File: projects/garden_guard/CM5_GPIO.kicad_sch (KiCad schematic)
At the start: 7 parts, among them J16 Conn_01x22_Female, J5 Conn_01x22_Female, J6 THD-02-R

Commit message: - Add 12V and 5V power sensing - Add solenoid and IR illum outputs, power expansion, an peripheral comms - General clean-up - Remove .bak files mistakenly added in previous commits - Add *.bak to .gitignore
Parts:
- removed J6: THD-02-R, Connector_PinHeader_2.54mm:PinHeader_2x02_P2.54mm_Vertical, symbol Connector_Generic:Conn_02x02_Odd_Even
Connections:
- net SCL1 is gone; now on net ID_SC: J16.20 (Pin_20), R7.2
- net SDA1 is gone; now on net ID_SD: J16.21 (Pin_21), R6.2
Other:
- note added: "CSI1 I2C Pull-Ups"
- note removed: "CSI1 Jumpers"
- note removed: "Jumper to enable CSI1 TODO: required?"
- note removed: "Jumpers to be fitted if DPHY1 is used"
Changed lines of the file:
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@@
 		(comment 4 "Adam Bowen")
 	)
-	(text "Jumper to enable CSI1\nTODO: required?"
+	(text "CSI1 I2C Pull-Ups"
 		(exclude_from_sim no)
-		(at 203.962 98.552 0)
-		(effects
-			(font
-				(size 1.27 1.27)
-				(thickness 0.1588)
-			)
-		)
-	)
-	(text "CSI1\nJumpers"
-		(exclude_from_sim no)
-		(at 179.324 102.362 0)
+		(at 193.04 103.632 0)
 		(effects
 			(font
@@
 		)
 	)
-	(text "Jumpers to be fitted if DPHY1 is used\n"
-		(exclude_from_sim no)
-		(at 223.52 130.556 0)
-		(effects
-			(font
-				(size 1.27 1.27)
-			)
-			(justify right bottom)
-		)
-	)
 	(text "CSI0"
 		(exclude_from_sim no)
@@
 		)
 	)
+	(text_box "CSI1 uses the HAT EEPROM ID I2C bus; we do not use HATs with this board, so we can use it.\n\nHAT ID bus does not have internal pull-up's specified, apply here."
+		(exclude_from_sim no)
+		(at 196.85 129.54 0)
+		(size 35.56 10.16)
+		(margins 0.9525 0.9525 0.9525 0.9525)
+		(stroke
+			(width 0)
+			(type solid)
+			(color 255 0 0 1)
+		)
+		(fill
+			(type none)
+		)
+		(effects
+			(font
+				(size 0.889 0.889)
+			)
+			(justify left)
+		)
+	)
 	(junction
 		(at 102.87 149.86)
@@
 	(polyline
 		(pts
-			(xy 177.8 93.98) (xy 228.6 93.98)
+			(xy 191.77 99.06) (xy 233.68 99.06)
 		)
 		(stroke
@@
 	(wire
 		(pts
-			(xy 198.12 106.68) (xy 208.28 106.68)
+			(xy 204.47 106.68) (xy 208.28 106.68)
 		)
 		(stroke
@@
 	(polyline
 		(pts
-			(xy 177.8 93.98) (xy 177.8 134.62)
+			(xy 191.77 99.06) (xy 191.77 140.97)
 		)
 		(stroke
@@
 	(polyline
 		(pts
-			(xy 177.8 134.62) (xy 228.6 134.62)
+			(xy 191.77 140.97) (xy 233.68 140.97)
 		)
 		(stroke
@@
 	(polyline
 		(pts
-			(xy 228.6 134.62) (xy 228.6 93.98)
+			(xy 233.68 140.97) (xy 233.68 93.98)
 		)
 		(stroke
@@
 	(wire
 		(pts
-			(xy 186.69 124.46) (xy 193.04 124.46)
-		)
-		(stroke
-			(width 0)
-			(type solid)
-		)
-	)
-	(wire
-		(pts
 			(xy 100.33 127) (xy 102.87 127)
 		)
@@
 	(wire
 		(pts
-			(xy 186.69 121.92) (xy 193.04 121.92)
-		)
-		(stroke
-			(width 0)
-			(type solid)
-		)
-	)
-	(wire
-		(pts
 			(xy 149.86 50.8) (xy 149.86 58.42)
 		)
@@
 		)
 	)
-	(label "ID_SC"
-		(at 192.405 121.92 180)
-		(effects
-			(font
-				(size 1.27 1.27)
-			)
-			(justify right bottom)
-		)
-	)
 	(label "DPHY1_D0_P"
 		(at 135.89 104.14 0)
@@
 		)
 	)
-	(label "SCL1"
-		(at 224.79 121.92 180)
-		(effects
-			(font
-				(size 1.27 1.27)
-			)
-			(justify right bottom)
-		)
-	)
 	(label "DPHY1_D2_P"
 		(at 116.84 147.32 180)
@@
 		)
 	)
-	(label "SDA1"
-		(at 135.89 149.86 0)
-		(effects
-			(font
-				(size 1.27 1.27)
-			)
-			(justify left bottom)
-		)
-	)
 	(label "DPHY0_D1_N"
 		(at 135.89 38.1 0)
@@
 		)
 	)
-	(label "SDA1"
-		(at 224.79 124.46 180)
-		(effects
-			(font
-				(size 1.27 1.27)
-			)
-			(justify right bottom)
-		)
-	)
 	(label "DPHY1_D2_N"
 		(at 116.84 144.78 180)
@@
 		)
 	)
-	(label "SCL1"
-		(at 135.89 147.32 0)
+	(label "ID_SD"
+		(at 135.89 149.86 0)
 		(effects
 			(font
@@
 		)
 	)
+	(label "ID_SC"
+		(at 135.89 147.32 0)
+		(effects
+			(font
+				(size 1.27 1.27)
+			)
+			(justify left bottom)
+		)
+	)
+	(label "ID_SC"
+		(at 205.74 121.92 180)
+		(effects
+			(font
+				(size 1.27 1.27)
+			)
+			(justify right bottom)
+		)
+	)
 	(label "DPHY1_C_N"
 		(at 135.89 116.84 0)
@@
 	)
 	(label "ID_SD"
-		(at 192.405 124.46 180)
+		(at 205.74 124.46 180)
 		(effects
 			(font
@@
 		)
 	)
+	(hierarchical_label "ID_SD"
+		(shape input)
+		(at 224.79 124.46 0)
+		(effects
+			(font
+				(size 1.27 1.27)
+			)
+			(justify left)
+		)
+	)
 	(hierarchical_label "SDA0"
 		(shape input)
@@
 		)
 	)
-	(hierarchical_label "ID_SD"
-		(shape input)
-		(at 186.69 124.46 180)
+	(hierarchical_label "PCIE_CLK_N"
+		(shape output)
+		(at 33.02 40.64 180)
 		(effects
 			(font
@@
 		)
 	)
-	(hierarchical_label "ID_SC"
+	(hierarchical_label "PCIE_RX_P"
 		(shape input)
-		(at 186.69 121.92 180)
-		(effects
-			(font
-				(size 1.27 1.27)
-			)
-			(justify right)
-		)
-	)
-	(hierarchical_label "PCIE_CLK_N"
-		(shape output)
-		(at 33.02 40.64 180)
+		(at 33.02 45.72 180)
 		(effects
 			(font
@@
 		)
 	)
-	(hierarchical_label "PCIE_RX_P"
+	(hierarchical_label "ID_SC"
 		(shape input)
-		(at 33.02 45.72 180)
+		(at 224.79 121.92 0)
 		(effects
 			(font
 				(size 1.27 1.27)
 			)
-			(justify right)
+			(justify left)
 		)
 	)
@@
 	(hierarchical_label "GPIO_VREF"
 		(shape input)
-		(at 198.12 106.68 180)
+		(at 204.47 106.68 180)
 		(effects
 			(font
@@
 				)
 			)
-		)
-	)
-	(symbol
-		(lib_id "Connector_Generic:Conn_02x02_Odd_Even")
-		(at 198.12 121.92 0)
-		(unit 1)
-		(exclude_from_sim no)
-		(in_bom yes)
-		(on_board yes)
-		(dnp no)
-		(property "Reference" "J6"
-			(at 195.453 116.713 0)
-			(effects
-				(font
-					(size 1.27 1.27)
-				)
-			)
-		)
-		(property "Value" "THD-02-R"
-			(at 199.39 118.7196 0)
-			(effects
-				(font
-					(size 1.27 1.27)
-				)
-			)
-		)
-		(property "Footprint" "Connector_PinHeader_2.54mm:PinHeader_2x02_P2.54mm_Vertical"
-			(at 198.12 121.92 0)
-			(effects
-				(font
-					(size 1.27 1.27)
-				)
-				(hide yes)
-			)
-		)
-		(property "Datasheet" "https://www.toby.co.uk/uploads/publications/1673.pdf"
-			(at 198.12 121.92 0)
-			(effects
-				(font
-					(size 1.27 1.27)
-				)
-				(hide yes)
-			)
-		)
-		(property "Description" ""
-			(at 198.12 121.92 0)
-			(effects
-				(font
-					(size 1.27 1.27)
-				)
-				(hide yes)
-			)
-		)
-		(property "Field4" "Toby"
-			(at 198.12 121.92 0)
-			(effects
-				(font
-					(size 1.27 1.27)
-				)
-				(hide yes)
-			)
-		)
-		(property "Field5" "THD-02-R"
-			(at 198.12 121.92 0)
-			(effects
-				(font
-					(size 1.27 1.27)
-				)
-				(hide yes)
-			)
-		)
-		(property "Field6" "151-604-425-761"
-			(at 198.12 121.92 0)
-			(effects
-				(font
-					(size 1.27 1.27)
-				)
-				(hide yes)
-			)
-		)
-		(property "Field7" "EDAC"
-			(at 198.12 121.92 0)
-			(effects
-				(font
-					(size 1.27 1.27)
-				)
-				(hide yes)
-			)
-		)
-		(property "Field8" "UCON00791"
-			(at 198.12 121.92 0)
-			(effects
-				(font
-					(size 1.27 1.27)
-				)
-				(hide yes)
-			)
-		)
-		(property "Part Description" "PinHeader_2x02_P2.54mm_Vertical"
-			(at 198.12 121.92 0)
-			(effects
-				(font
-					(size 1.27 1.27)
-				)
-				(hide yes)
-			)
-		)
-		(pin "1"
-		)
-		(pin "2"
-		)
-		(pin "3"
-		)
-		(pin "4"
-		)
-		(instances
-			(project "garden_guard"
-				(path "/dcdac9d4-ef08-426f-b97c-7b9219501e71/ffd8c860-2f3d-4401-ad04-ed468bcbcf5a"
-					(reference "J6")
-					(unit 1)
-				)
-			)

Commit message: - Add all missing footprints - Add specific part numbers to each component in schematic
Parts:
- renumbered J16 to J6, R6 to R10, R7 to R11, R8 to R9
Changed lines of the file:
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@@
 		(on_board yes)
 		(dnp no)
-		(property "Reference" "#PWR0130"
+		(property "Reference" "#PWR015"
 			(at 102.87 161.29 0)
 			(effects
@@
 			(project "garden_guard"
 				(path "/dcdac9d4-ef08-426f-b97c-7b9219501e71/ffd8c860-2f3d-4401-ad04-ed468bcbcf5a"
-					(reference "#PWR0130")
+					(reference "#PWR015")
 					(unit 1)
 				)
@@
 		(on_board yes)
 		(dnp no)
-		(property "Reference" "#PWR0131"
+		(property "Reference" "#PWR014"
 			(at 36.83 161.29 0)
 			(effects
@@
 			(project "garden_guard"
 				(path "/dcdac9d4-ef08-426f-b97c-7b9219501e71/ffd8c860-2f3d-4401-ad04-ed468bcbcf5a"
-					(reference "#PWR0131")
+					(reference "#PWR014")
 					(unit 1)
 				)
@@
 		(on_board yes)
 		(dnp no)
-		(property "Reference" "#PWR0134"
+		(property "Reference" "#PWR016"
 			(at 149.86 88.9 0)
 			(effects
@@
 			(project "garden_guard"
 				(path "/dcdac9d4-ef08-426f-b97c-7b9219501e71/ffd8c860-2f3d-4401-ad04-ed468bcbcf5a"
-					(reference "#PWR0134")
+					(reference "#PWR016")
 					(unit 1)
 				)
@@
 		(on_board yes)
 		(dnp no)
-		(property "Reference" "#PWR0135"
+		(property "Reference" "#PWR017"
 			(at 149.86 160.02 0)
 			(effects
@@
 			(project "garden_guard"
 				(path "/dcdac9d4-ef08-426f-b97c-7b9219501e71/ffd8c860-2f3d-4401-ad04-ed468bcbcf5a"
-					(reference "#PWR0135")
+					(reference "#PWR017")
 					(unit 1)
 				)
@@
 		(on_board yes)
 		(dnp no)
-		(property "Reference" "R6"
+		(property "Reference" "R10"
 			(at 203.708 111.125 0)
 			(effects
@@
 			(project "garden_guard"
 				(path "/dcdac9d4-ef08-426f-b97c-7b9219501e71/ffd8c860-2f3d-4401-ad04-ed468bcbcf5a"
-					(reference "R6")
+					(reference "R10")
 					(unit 1)
 				)
@@
 		(on_board yes)
 		(dnp no)
-		(property "Reference" "R7"
+		(property "Reference" "R11"
 			(at 217.678 111.125 0)
 			(effects
@@
 			(project "garden_guard"
 				(path "/dcdac9d4-ef08-426f-b97c-7b9219501e71/ffd8c860-2f3d-4401-ad04-ed468bcbcf5a"
-					(reference "R7")
+					(reference "R11")
 					(unit 1)
 				)
@@
 		(on_board yes)
 		(dnp no)
-		(property "Reference" "J16"
+		(property "Reference" "J6"
 			(at 134.62 95.25 0)
 			(effects
@@
 			(project "garden_guard"
 				(path "/dcdac9d4-ef08-426f-b97c-7b9219501e71/ffd8c860-2f3d-4401-ad04-ed468bcbcf5a"
-					(reference "J16")
+					(reference "J6")
 					(unit 1)
 				)
@@
 		(on_board yes)
 		(dnp no)
-		(property "Reference" "R8"
+		(property "Reference" "R9"
 			(at 137.795 137.16 90)
 			(effects
@@
 			(project "garden_guard"
 				(path "/dcdac9d4-ef08-426f-b97c-7b9219501e71/ffd8c860-2f3d-4401-ad04-ed468bcbcf5a"
-					(reference "R8")
+					(reference "R9")
 					(unit 1)
 				)

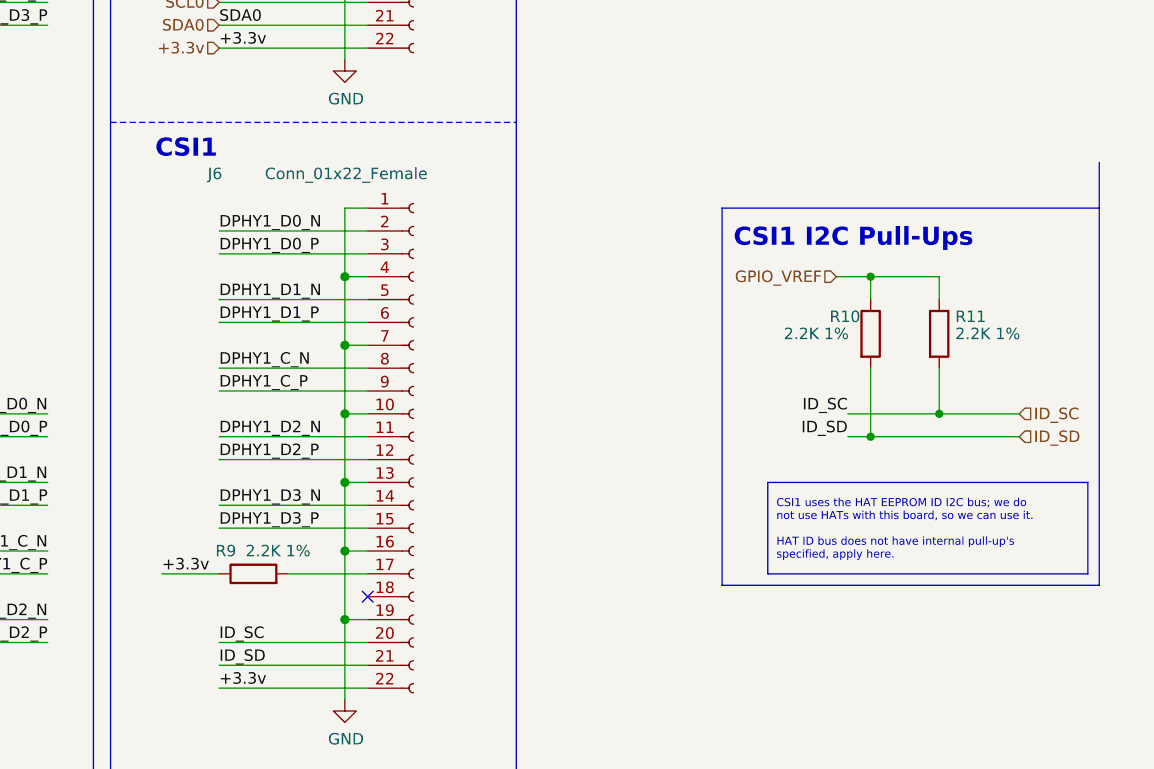
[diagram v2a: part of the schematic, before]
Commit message: - Find part numbers for CM5 parts - Minor CM5 symbol, footprint adjustments - Move to uniform small resistor and capacitor symbols - Add *lck to .gitignore
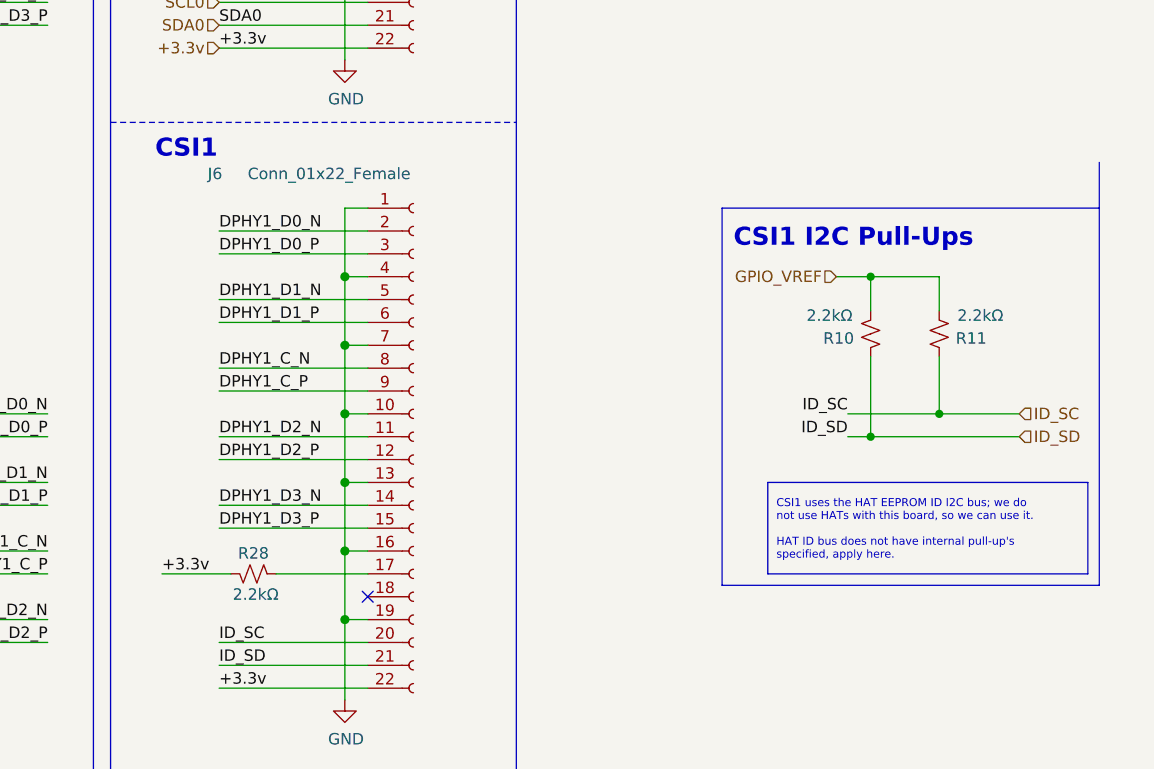
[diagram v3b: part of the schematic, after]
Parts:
- removed R10, R11, R9: 2.2K 1%, Resistor_SMD:R_0402_1005Metric, symbol Device:R
- added R10, R11, R28: 2.2kΩ, Capacitor_SMD:C_0603_1608Metric, symbol Device:R_Small_US
- J5, J6: MPN (none) -> FH12-22S-0.5SH(55); Mfr (none) -> Hirose
- Module1: MPN (none) -> 10164227-1004A1RLF; Mfr (none) -> Amphenol
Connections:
- net +3.3v: now also R28.2
- net GPIO_VREF: now also R10.1, R11.1
- net ID_SC: now also R11.2
- net ID_SD: now also R10.2
- net at J6.17 (Pin_17): now also R28.1

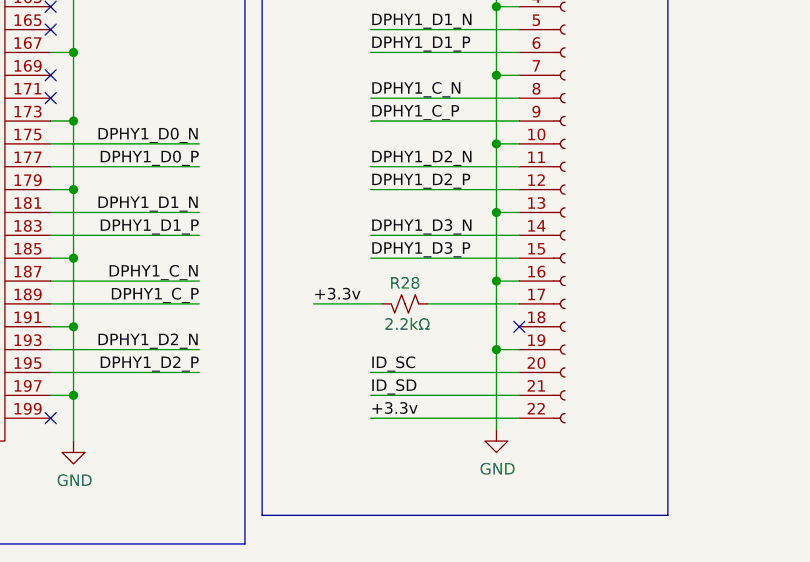
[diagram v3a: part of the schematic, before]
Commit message: - Assign 3D models to lingering footprints lacking them - Start playing with board layout - Move CM5 library files from project to components dir
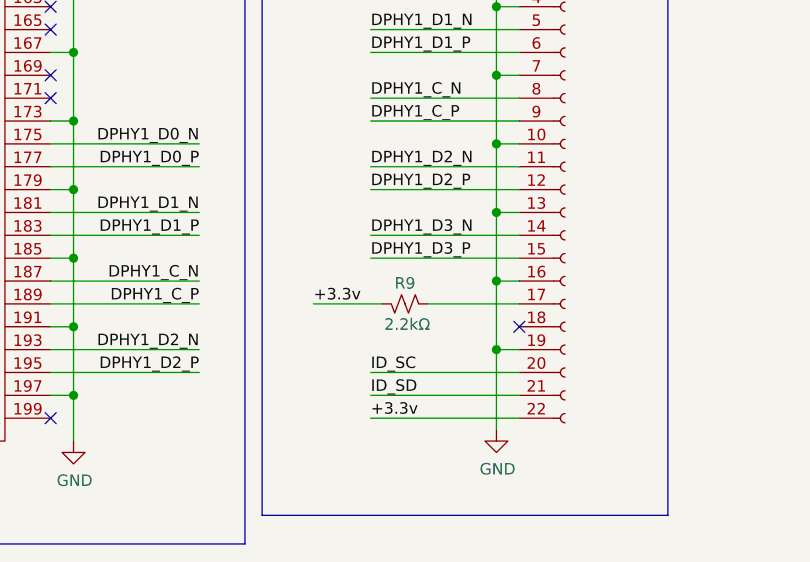
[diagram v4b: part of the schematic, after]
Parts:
- Module1: footprint CM5IO:Raspberry-Pi-5-Compute-Module -> CM5IO:Raspberry-Pi-5-Compute-Module_tall
- renumbered R28 to R9
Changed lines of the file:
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@@
 			)
 		)
-		(property "Footprint" "CM5IO:Raspberry-Pi-5-Compute-Module"
+		(property "Footprint" "CM5IO:Raspberry-Pi-5-Compute-Module_tall"
 			(at 72.39 115.57 0)
 			(effects
@@
 		(on_board yes)
 		(dnp no)
-		(property "Reference" "R28"
+		(property "Reference" "R9"
 			(at 139.7 137.414 90)
 			(effects
@@
 			(project "garden_guard"
 				(path "/dcdac9d4-ef08-426f-b97c-7b9219501e71/ffd8c860-2f3d-4401-ad04-ed468bcbcf5a"
-					(reference "R28")
+					(reference "R9")
 					(unit 1)
 				)

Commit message: - Add M.2 power and connector layout - Add micro HDMI to schematic and layout - Add microSD layout - Add IR illuminator and solenoid output MOSFET layouts - Add USB-C layout
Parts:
- added C31, C32: 0.1uF, Resistor_SMD:R_0603_1608Metric, symbol Device:C_Small
- added J22: 10118242-001RLF, Custom_Connector:10118242-001RLF, symbol CM5IO:HDMI_A_1.4
- added U14: RT9742SNGV, Package_TO_SOT_SMD:TSOT-23_HandSoldering, symbol CM5IO:RT9742SNGV
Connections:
- net GND: now also C31.2, C32.2, J22.11 (CKS), J22.17 (GND), J22.2 (D2S), J22.5 (D1S), J22.8 (D0S), J22.SH1 (SH), J22.SH2 (SH), J22.SH3 (SH), J22.SH4 (SH), U14.3 (GND)
- net HDMI0_CEC: now reaches Module1.151 (HDMI0_CEC)
- net HDMI0_CEC: now also J22.13 (CEC)
- net HDMI0_HOTPLUG: now reaches Module1.153 (HDMI0_HOTPLUG)
- net HDMI0_HOTPLUG: now also J22.19 (HPD/HEAC-)
- net HDMI0_D2_P: now reaches Module1.170 (HDMI0_TX2_P)
- net HDMI0_D2_P: now also J22.1 (D2+)
- net HDMI0_D2_N: now reaches Module1.172 (HDMI0_TX2_N)
- net HDMI0_D2_N: now also J22.3 (D2-)
- net HDMI0_D1_P: now reaches Module1.176 (HDMI0_TX1_P)
- net HDMI0_D1_P: now also J22.4 (D1+)
- net HDMI0_D1_N: now reaches Module1.178 (HDMI0_TX1_N)
- net HDMI0_D1_N: now also J22.6 (D1-)
- net HDMI0_D0_P: now reaches Module1.182 (HDMI0_TX0_P)
- net HDMI0_D0_P: now also J22.7 (D0+)
- net HDMI0_D0_N: now reaches Module1.184 (HDMI0_TX0_N)
- net HDMI0_D0_N: now also J22.9 (D0-)
- net HDMI0_CK_P: now reaches Module1.188 (HDMI0_CLK_P)
- net HDMI0_CK_P: now also J22.10 (CK+)
- net HDMI0_CK_N: now reaches Module1.190 (HDMI0_CLK_N)
- net HDMI0_CK_N: now also J22.12 (CK-)
- net HDMI0_SDA: now reaches Module1.199 (HDMI0_SDA)
- net HDMI0_SDA: now also J22.16 (SDA)
- net HDMI0_SCL: now reaches Module1.200 (HDMI0_SCL)
- net HDMI0_SCL: now also J22.15 (SCL)
- new net +5v: C31.1, U14.1 (IN)
- new net HDMI_5v: C32.1, J22.18 (+5V), U14.2 (OUT)
- no-connect marks 38 -> 27
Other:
- note added: "HDMI Connector"
- note added: "HDMI Power"
- moved on the sheet: R10, R11

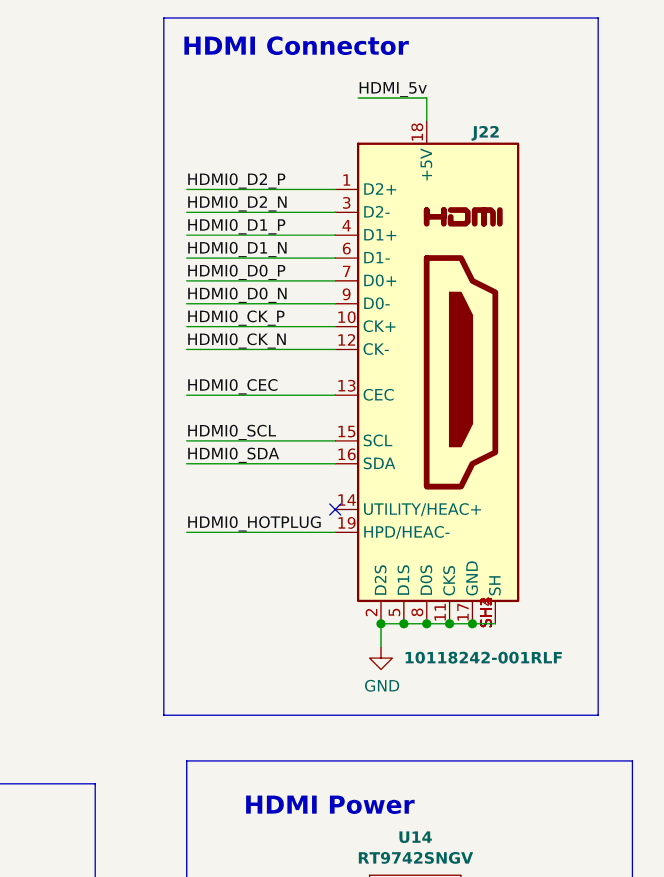
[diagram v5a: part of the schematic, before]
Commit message: - Replace micro HDMI with mini HDMI - Start arrangement of sub-layouts
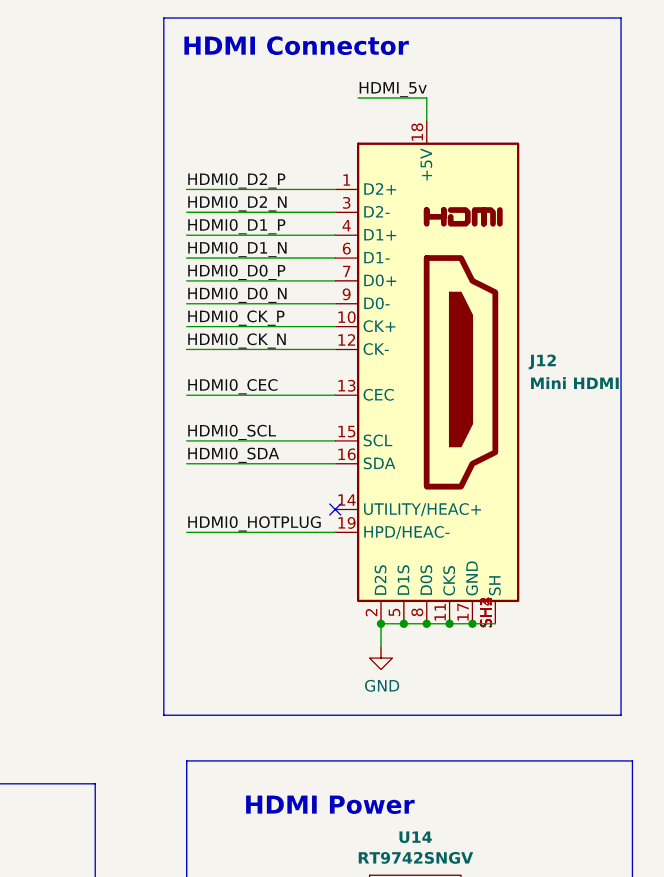
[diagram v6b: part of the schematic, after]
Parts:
- removed J22: 10118242-001RLF, Custom_Connector:10118242-001RLF, symbol CM5IO:HDMI_A_1.4
- added J12: Mini HDMI, Custom_Connector:2013978-2, symbol Custom_Connector:Mini_HDMI
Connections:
- net GND: now also J12.11 (CKS), J12.17 (GND), J12.2 (D2S), J12.5 (D1S), J12.8 (D0S), J12.SH1 (SH), J12.SH2 (SH), J12.SH3 (SH), J12.SH4 (SH)
- net HDMI0_CEC: now also J12.13 (CEC)
- net HDMI0_CK_N: now also J12.12 (CK-)
- net HDMI0_CK_P: now also J12.10 (CK+)
- net HDMI0_D0_N: now also J12.9 (D0-)
- net HDMI0_D0_P: now also J12.7 (D0+)
- net HDMI0_D1_N: now also J12.6 (D1-)
- net HDMI0_D1_P: now also J12.4 (D1+)
- net HDMI0_D2_N: now also J12.3 (D2-)
- net HDMI0_D2_P: now also J12.1 (D2+)
- net HDMI0_HOTPLUG: now also J12.19 (HPD/HEAC-)
- net HDMI0_SCL: now also J12.15 (SCL)
- net HDMI0_SDA: now also J12.16 (SDA)
- net HDMI_5v: now also J12.18 (+5V)
